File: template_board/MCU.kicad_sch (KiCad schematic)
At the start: 37 parts, among them J1 SWD, SW1 BOOT0, SW2 NRST, SW3 USR_BTN, U2 FM24CL16B, U9 STM32F446RETx, Y1 8MHz, Y3 32.768kHz

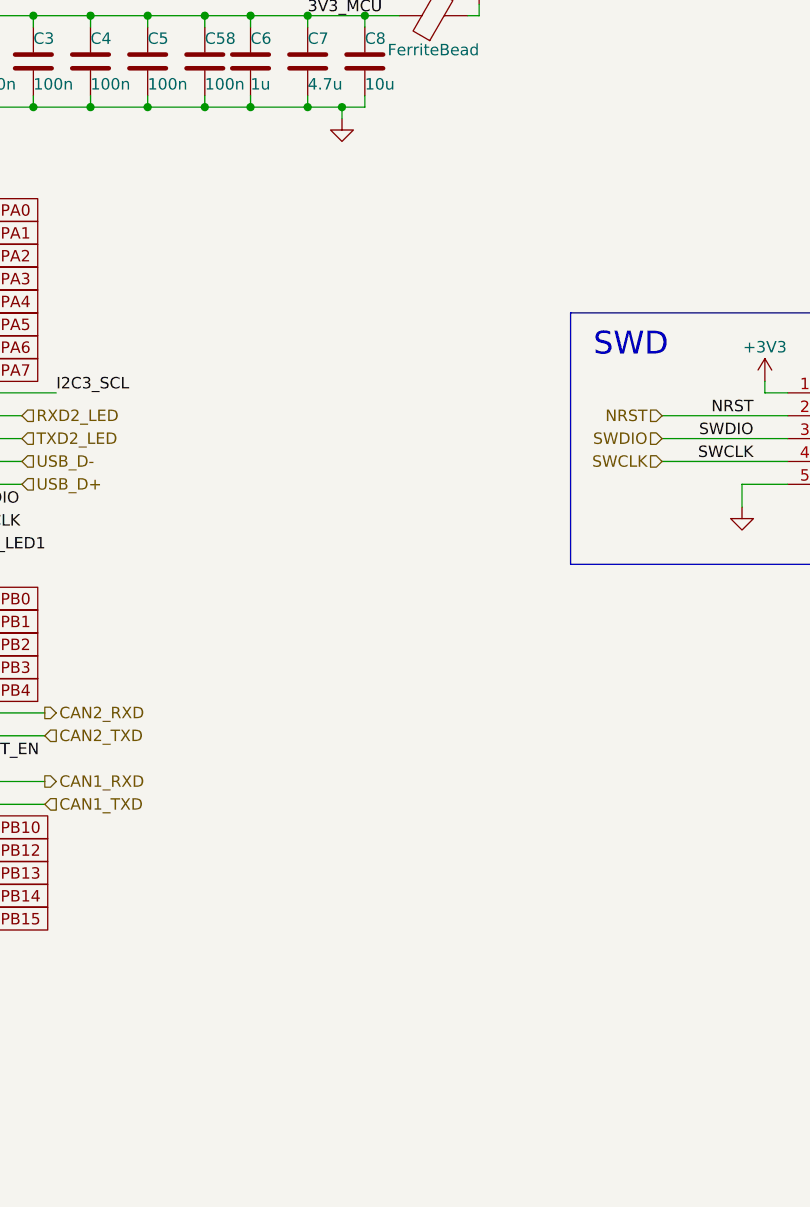
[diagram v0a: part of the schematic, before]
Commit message: added newm mcu on a  side
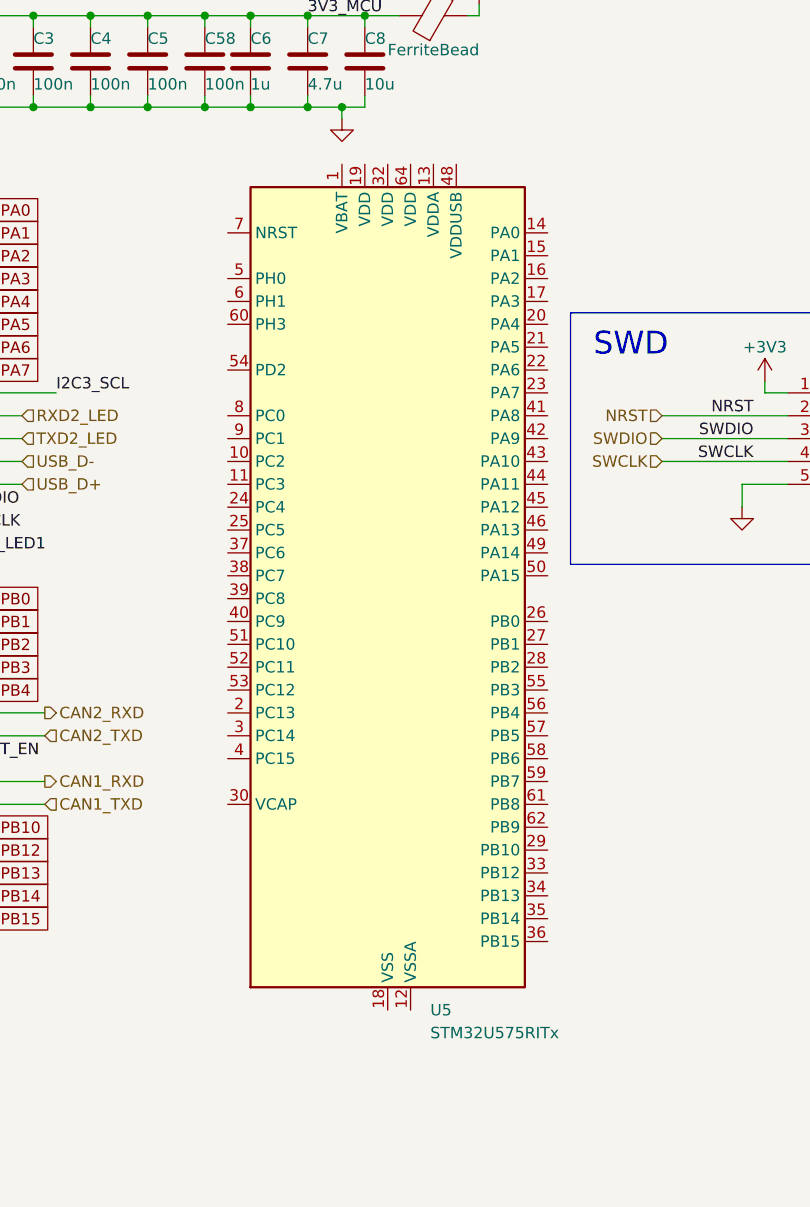
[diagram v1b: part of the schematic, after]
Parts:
- added U5: STM32U575RITx, Package_QFP:LQFP-64_10x10mm_P0.5mm, symbol MCU_ST_STM32U5:STM32U575RITx
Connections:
- new net: U5.18 (VSS), U5.31 (VSS), U5.47 (VSS), U5.63 (VSS)
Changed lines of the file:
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@@
+	)
+	(symbol
+		(lib_id "MCU_ST_STM32U5:STM32U575RITx")
+		(at 222.25 97.79 0)
+		(unit 1)
+		(exclude_from_sim no)
+		(in_bom yes)
+		(on_board yes)
+		(dnp no)
+		(fields_autoplaced yes)
+		(property "Reference" "U5"
+			(at 226.9841 143.51 0)
+			(effects
+				(font
+					(size 1.27 1.27)
+				)
+				(justify left)
+			)
+		)
+		(property "Value" "STM32U575RITx"
+			(at 226.9841 146.05 0)
+			(effects
+				(font
+					(size 1.27 1.27)
+				)
+				(justify left)
+			)
+		)
+		(property "Footprint" "Package_QFP:LQFP-64_10x10mm_P0.5mm"
+			(at 207.01 140.97 0)
+			(effects
+				(font
+					(size 1.27 1.27)
+				)
+				(justify right)
+				(hide yes)
+			)
+		)
+		(property "Datasheet" "https://www.st.com/resource/en/datasheet/stm32u575ri.pdf"
+			(at 222.25 97.79 0)
+			(effects
+				(font
+					(size 1.27 1.27)
+				)
+				(hide yes)
+			)
+		)
+		(property "Description" "STMicroelectronics Arm Cortex-M33 MCU, 2048KB flash, 786KB RAM, 160 MHz, 1.71-3.6V, 51 GPIO, LQFP64"
+			(at 222.25 97.79 0)
+			(effects
+				(font
+					(size 1.27 1.27)
+				)
+				(hide yes)
+			)
+		)
+		(pin "36"
+		)
+		(pin "16"
+		)
+		(pin "58"
+		)
+		(pin "6"
+		)
+		(pin "35"
+		)
+		(pin "38"
+		)
+		(pin "57"
+		)
+		(pin "37"
+		)
+		(pin "25"
+		)
+		(pin "51"
+		)
+		(pin "32"
+		)
+		(pin "34"
+		)
+		(pin "60"
+		)
+		(pin "42"
+		)
+		(pin "4"
+		)
+		(pin "23"
+		)
+		(pin "44"
+		)
+		(pin "22"
+		)
+		(pin "39"
+		)
+		(pin "20"
+		)
+		(pin "41"
+		)
+		(pin "40"
+		)
+		(pin "56"
+		)
+		(pin "55"
+		)
+		(pin "59"
+		)
+		(pin "31"
+		)
+		(pin "3"
+		)
+		(pin "47"
+		)
+		(pin "28"
+		)
+		(pin "62"
+		)
+		(pin "46"
+		)
+		(pin "64"
+		)
+		(pin "53"
+		)
+		(pin "9"
+		)
+		(pin "43"
+		)
+		(pin "2"
+		)
+		(pin "18"
+		)
+		(pin "24"
+		)
+		(pin "21"
+		)
+		(pin "29"
+		)
+		(pin "26"
+		)
+		(pin "5"
+		)
+		(pin "63"
+		)
+		(pin "11"
+		)
+		(pin "12"
+		)
+		(pin "13"
+		)
+		(pin "48"
+		)
+		(pin "7"
+		)
+		(pin "61"
+		)
+		(pin "52"
+		)
+		(pin "33"
+		)
+		(pin "8"
+		)
+		(pin "27"
+		)
+		(pin "17"
+		)
+		(pin "45"
+		)
+		(pin "30"
+		)
+		(pin "54"
+		)
+		(pin "49"
+		)
+		(pin "14"
+		)
+		(pin "15"
+		)
+		(pin "1"
+		)
+		(pin "19"
+		)
+		(pin "50"
+		)
+		(pin "10"
+		)
+		(instances
+			(project ""
+				(path "/f131027f-631c-4099-b0ec-5f883860005f/a4b9441c-60f3-49e8-82a9-f2ebbfa51587"
+					(reference "U5")
+					(unit 1)
+				)
+			)
+		)
 	)
 	(symbol

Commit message: u5 wip
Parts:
- removed C1, C2, C3, C4, C5, C58, C9: 100n, Capacitor_SMD:C_0402_1005Metric, symbol Device:C
- removed C10: 4.7u, Capacitor_SMD:C_0402_1005Metric, symbol Device:C
- removed C6: 1u, Capacitor_SMD:C_0603_1608Metric, symbol Device:C
- removed C7: 4.7u, Capacitor_SMD:C_0603_1608Metric, symbol Device:C
- removed C8: 10u, Capacitor_SMD:C_0805_2012Metric, symbol Device:C
- removed FB1: FerriteBead, Inductor_SMD:L_0805_2012Metric, symbol Device:FerriteBead
- removed J1: SWD, Connector_PinSocket_2.54mm:PinSocket_1x05_P2.54mm_Vertical, symbol Connector_Generic:Conn_01x05
- removed R10, R3, R9: 1k, Resistor_SMD:R_0402_1005Metric, symbol Device:R
- removed R4, R7, R8: 10k, Resistor_SMD:R_0402_1005Metric, symbol Device:R
- removed R5, R6: 4k7, Resistor_SMD:R_0402_1005Metric, symbol Device:R
- removed SW1: BOOT0, Button_Switch_THT:SW_Tactile_SPST_Angled_PTS645Vx58-2LFS, symbol Switch:SW_Push
- removed SW2: NRST, Button_Switch_THT:SW_Tactile_SPST_Angled_PTS645Vx58-2LFS, symbol Switch:SW_Push
- removed SW3: USR_BTN, Button_Switch_THT:SW_Tactile_SPST_Angled_PTS645Vx58-2LFS, symbol Switch:SW_Push
- removed U2: FM24CL16B, Package_SO:SOIC-8_3.9x4.9mm_P1.27mm, symbol custom_symbols:FM24CL16B
- added C10, C28, C29, C30, C9: 100nF, PCM_JLCPCB:C_0402, symbol PCM_JLCPCB-Capacitors:0402,100nF
- added C31: 1uF, PCM_JLCPCB:C_0402, symbol PCM_JLCPCB-Capacitors:0402,1uF
- added C32: 10nF, PCM_JLCPCB:C_0402, symbol PCM_JLCPCB-Capacitors:0402,10nF
- added C50: 4.7uF, PCM_JLCPCB:C_0402, symbol PCM_JLCPCB-Capacitors:0402,4.7uF
- added C60: 4.7u, Capacitor_SMD:C_0402_1005Metric, symbol Device:C
- added C61: 100n, symbol Device:C
- added FB2: FerriteBead, Inductor_SMD:L_0805_2012Metric, symbol Device:FerriteBead
- added J3: SWD, Connector_PinSocket_2.54mm:PinSocket_1x05_P2.54mm_Vertical, symbol Connector_Generic:Conn_01x05
- added R25: 1k, symbol Device:R
- added R26, R28: 10k, symbol Device:R
- added SW6: NRST, Button_Switch_THT:SW_Tactile_SPST_Angled_PTS645Vx58-2LFS, symbol Switch:SW_Push
- R1: now fitted
- R2: value 10k -> 1k
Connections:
- net +3V3: now also FB2.1, J3.1 (Pin_1), R28.1; no longer R2.1
- net BOOT0: now also C60.1, R25.2, R26.1; no longer R1.2
- net BOOT_EN: now also U5.59 (PB7), R25.1
- net GND: now also U5.12 (VSSA), U5.18 (VSS), U5.31 (VSS), U5.47 (VSS), U5.63 (VSS), C10.2, C28.2, C29.2, C30.2, C31.2, C32.2, C50.2, C60.2, C61.2, C9.2, J3.5 (Pin_5), R26.2, SW6.1
- net NRST: now also U5.7 (NRST), C61.1, J3.2 (Pin_2), R28.2, SW6.2; no longer R2.2
- net SWCLK: now also U5.49 (PA14), J3.4 (Pin_4)
- net SWDIO: now also U5.46 (PA13), J3.3 (Pin_3)
- net USB_D+: now also U5.45 (PA12)
- net USB_D-: now also U5.44 (PA11)
- net USR_LED1: now also R1.1, U5.50 (PA15), U5.51 (PC10)
- net USR_LED2: now also R2.1
- net at D2.2 (A): now also R1.2
- net at U5.1 (VBAT): now also U5.13 (VDDA), U5.19 (VDD), U5.32 (VDD), U5.48 (VDDUSB), U5.64 (VDD), C10.1, C28.1, C29.1, C30.1, C31.1, C32.1, C9.1, FB2.2
- net at U5.30 (VCAP): now also C50.1
- net FDCAN_RX: now reaches U5.41 (PA8)
- net FDCAN_TX: now reaches U5.42 (PA9)
- net BOOT: now reaches U5.60 (PH3)
- net at D3.2 (A): now also R2.2
- removed net 3V3_MCU: U9.1 (VBAT), U9.13 (VDDA), U9.19 (VDD), U9.32 (VDD), U9.48 (VDD), U9.64 (VDD)
- no-connect marks 3 -> 0
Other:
- note removed: "FRAM"
- note removed: "I2C"
- note removed: "USER BUTTON"
- moved on the sheet: U5

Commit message: u5 wip
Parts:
- removed C60: 4.7u, Capacitor_SMD:C_0402_1005Metric, symbol Device:C
- removed C61: 100n, symbol Device:C
- removed D2: USR_LED1, Diode_SMD:D_0603_1608Metric, symbol Device:LED
- removed D3: USR_LED2, Diode_SMD:D_0603_1608Metric, symbol Device:LED
- removed FB2: FerriteBead, Inductor_SMD:L_0805_2012Metric, symbol Device:FerriteBead
- removed R1, R2: 1k, Resistor_SMD:R_0402_1005Metric, symbol Device:R
- removed R25: 1k, symbol Device:R
- removed R26, R28: 10k, symbol Device:R
- added C1: 4.7uF, PCM_JLCPCB:C_0402, symbol PCM_JLCPCB-Capacitors:0402,4.7uF
- added C2: 100nF, PCM_JLCPCB:C_0402, symbol PCM_JLCPCB-Capacitors:0402,100nF
- added D2, D6: Green, PCM_JLCPCB:D_0805, symbol PCM_JLCPCB-Diodes:LED,0805,Green
- added FB1: ~, PCM_JLCPCB:FB_0603, symbol PCM_JLCPCB-Inductors:Ferrite,0603
- added R1, R2, R3: 1kΩ, PCM_JLCPCB:R_0402, symbol PCM_JLCPCB-Resistors:0402,1kΩ
- added R4, R5: 10kΩ, PCM_JLCPCB:R_0402, symbol PCM_JLCPCB-Resistors:0402,10kΩ
- added X1: X50328MSB2GI, PCM_JLCPCB:CRYSTAL-SMD_L5.0-W3.2, symbol PCM_JLCPCB-Crystals:Crystal, 8MHz, 20pF, ±10ppm
- added X2: Q13FC1350000400, PCM_JLCPCB:FC-135R_L3.2-W1.5, symbol PCM_JLCPCB-Crystals:Crystal, 32.768kHz, 13pF
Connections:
- net +3V3: now also FB1.1, R5.1
- net BOOT0: now also C1.1, R3.2, R4.1
- net BOOT_EN: now also R3.1
- net GND: now also C1.2, C2.2, D2.1, D6.1, R4.2
- net NRST: now also C2.1, R5.2
- net USR_LED1: now also R1.1
- net USR_LED2: now also R2.2
- net at C10.1, C28.1, C29.1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: now also FB1.2
- new net: D2.2, R2.1
- new net: D6.2, R1.2

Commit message: updated all subschematics
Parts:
- removed C11, C12: 17p, Capacitor_SMD:C_0402_1005Metric, symbol Device:C
- removed C55: 2.2u, Capacitor_SMD:C_0402_1005Metric, symbol Device:C
- removed C56, C57: 6P, Capacitor_SMD:C_0402_1005Metric, symbol Device:C
- removed D2, D6: Green, PCM_JLCPCB:D_0805, symbol PCM_JLCPCB-Diodes:LED,0805,Green
- removed R1, R2: 1kΩ, PCM_JLCPCB:R_0402, symbol PCM_JLCPCB-Resistors:0402,1kΩ
- removed U9: STM32F446RETx, Package_QFP:LQFP-64_10x10mm_P0.5mm, symbol MCU_ST_STM32F4:STM32F446RETx
- removed X1: X50328MSB2GI, PCM_JLCPCB:CRYSTAL-SMD_L5.0-W3.2, symbol PCM_JLCPCB-Crystals:Crystal, 8MHz, 20pF, ±10ppm
- removed X2: Q13FC1350000400, PCM_JLCPCB:FC-135R_L3.2-W1.5, symbol PCM_JLCPCB-Crystals:Crystal, 32.768kHz, 13pF
- removed Y1: 8MHz, Crystal:Crystal_SMD_3225-4Pin_3.2x2.5mm, symbol Device:Crystal_GND24
- removed Y3: 32.768kHz, Crystal:Crystal_SMD_3215-2Pin_3.2x1.5mm, symbol Device:Crystal
- added C51, C59: 18pF, PCM_JLCPCB:C_0402, symbol PCM_JLCPCB-Capacitors:0402,18pF
- added C58, C60: 22pF, PCM_JLCPCB:C_0402, symbol PCM_JLCPCB-Capacitors:0402,22pF
- added D11, D7: Red, PCM_JLCPCB:D_0603, symbol PCM_JLCPCB-Diodes:LED,0603,Red
- added D12, D2: Blue, PCM_JLCPCB:D_0603, symbol PCM_JLCPCB-Diodes:LED,0603,Blue
- added R27: 10kΩ, PCM_JLCPCB:R_0402, symbol PCM_JLCPCB-Resistors:0402,10kΩ
- added R29: 1k, Resistor_SMD:R_0402_1005Metric, symbol Device:R
- added R30, R69: 1.2kΩ, PCM_JLCPCB:R_0402, symbol PCM_JLCPCB-Resistors:0402,1.2kΩ
- added R63: 470Ω, PCM_JLCPCB:R_0402, symbol PCM_JLCPCB-Resistors:0402,470Ω
- added R70: 120Ω, PCM_JLCPCB:R_0402, symbol PCM_JLCPCB-Resistors:0402,120Ω
- added X3: Q13FC1350000400, PCM_JLCPCB:FC-135R_L3.2-W1.5, symbol PCM_JLCPCB-Crystals:Crystal, 32.768kHz, 13pF
- added X4: X322512MSB4SI, PCM_JLCPCB:CRYSTAL-SMD_4P-L3.2-W2.5-BL, symbol PCM_JLCPCB-Crystals:Crystal, 12MHz, 20pF
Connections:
- net +3V3: now also R70.1
- net GND: now also C51.2, C58.2, C59.2, C60.2, D11.1, D12.1, D2.1, D7.1, R29.2, X4.2, X4.4
- net V_SENSE: now also U5.8 (PC0), R27.2, R29.1
- net +VDDA: now reaches C10.1, C28.1, C29.1, C30.1, C31.1, C32.1, C9.1, FB1.2, U5.1 (VBAT), U5.13 (VDDA), U5.19 (VDD), U5.32 (VDD), U5.48 (VDDUSB), U5.64 (VDD)
- net OSC32_IN: now reaches U5.3 (PC14)
- net OSC32_IN: now also C59.1, X3.2
- net OSC32_OUT: now reaches U5.4 (PC15)
- net OSC32_OUT: now also C51.1, X3.1
- net OSC_IN: now reaches U5.5 (PH0)
- net OSC_IN: now also C58.1, X4.1
- net OSC_OUT: now reaches U5.6 (PH1)
- net OSC_OUT: now also C60.1, X4.3
- net CAN.RX: now reaches U5.61 (PB8)
- net CAN.TX: now reaches U5.62 (PB9)
- net FDCAN_RX: no longer names the net of U5.41 (PA8)
- net FDCAN_TX: no longer names the net of U5.42 (PA9)
- net NRST renamed SWD.~{RST}
- net SWCLK renamed SWD.SWCLK
- net SWDIO renamed SWD.SWDIO
- net USB_D+ renamed USB_MCU.D+
- net USB_D- renamed USB_MCU.D-
- net USR_LED1: no longer names the net of U5.50 (PA15)
- net USR_LED1: no longer U5.51 (PC10)
- new net: D7.2, R63.2
- new net: D2.2, R69.2
- new net: D12.2, R30.2
- new net: D11.2, R70.2
- new net +5V: R27.1
- new net STATUS_LED: R63.1
- new net USER_LED_1: R30.1
- new net USER_LED_2: R69.1
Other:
- note added: "BOOT/RESET"
- note added: "CRYSTAL RESONATORS"
- note added: "POWER INDICATOR AND USER LEDs"
- note added: "POWER SENSE"
- note added: "Target I_{LED} = 5mA"
- note removed: "Boot Reset"
- note removed: "C_{L} = 9p C_{S} ~ 3p C_{L1} * C_{L2} / (C_{L1} + C_{L2}) = = C_{L} - C_{S} C_{L1} = C_{L2} -> (14-18)p"
- note removed: "TO 6p resonator"
- note removed: "USER LED"
- moved on the sheet: C1, C10, C2, C28, C29, C30, C31, C32, C50, C9, FB1, J3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

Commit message: chamt skończony chyba
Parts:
- removed D11: Red, PCM_JLCPCB:D_0603, symbol PCM_JLCPCB-Diodes:LED,0603,Red
- removed R70: 120Ω, PCM_JLCPCB:R_0402, symbol PCM_JLCPCB-Resistors:0402,120Ω
- removed SW6: NRST, Button_Switch_THT:SW_Tactile_SPST_Angled_PTS645Vx58-2LFS, symbol Switch:SW_Push
- added SW1: SW_Push, lib:TS1088R02026, symbol Switch:SW_Push
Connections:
- net GND: now also SW1.1
- net SWD.~{RST}: now also SW1.2
- net CAN_TRANSIVER.CLK: now reaches U5.55 (PB3)
- net CAN_TRANSIVER.MISO: now reaches U5.56 (PB4)
- net CAN_TRANSIVER.MOSI: now reaches U5.57 (PB5)
- net CAN_TRANSIVER.CS: now reaches U5.58 (PB6)

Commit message: schemat skończony
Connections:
- net STLINK_UART.RX: now reaches U5.51 (PC10)
- net STLINK_UART.TX: now reaches U5.52 (PC11)
- no-connect marks 0 -> 32

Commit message: stated leyout
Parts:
- removed J3: SWD, Connector_PinSocket_2.54mm:PinSocket_1x05_P2.54mm_Vertical, symbol Connector_Generic:Conn_01x05
- removed R29: 1k, Resistor_SMD:R_0402_1005Metric, symbol Device:R
- added C4: 100nF, PCM_JLCPCB:C_0402, symbol PCM_JLCPCB-Capacitors:0402,100nF
- added R6: 1kΩ, PCM_JLCPCB:R_0402, symbol PCM_JLCPCB-Resistors:0402,1kΩ
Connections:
- net BOOT0 is gone; now on net BOOT: C1.1, R3.2, R4.1
- net +VDDA: now also C4.1
- net GND: now also C4.2, R6.2
- net STATUS_LED: now also U5.41 (PA8)
- net USER_LED_1: now also U5.43 (PA10)
- net USER_LED_2: now also U5.42 (PA9)
- net V_SENSE: now also R6.1
- no-connect marks 32 -> 29
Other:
- note removed: "SWD"
- moved on the sheet: C10, C9
